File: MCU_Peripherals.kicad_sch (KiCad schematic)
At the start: 108 parts, among them J1 Conn_02x04_Odd_Even, J101 Conn_01x06_Male, J102 Conn_01x06_Male, J2 DS1023-2*8SF11, J20 DS1023-2*8SF11, J200 Conn_ARM_JTAG_SWD_10, J4 Conn_ARM_JTAG_SWD_10, J5 Conn_01x03_Female, J6 Conn_01x02, Q1 IRLR8726TRPBF, Q10 IRLR8726TRPBF, Q2 IRLR8726TRPBF, Q3 IRLR8726TRPBF, Q4 IRLR8726TRPBF, Q5 IRLR8726TRPBF, Q6 IRLR8726TRPBF, Q7 IRLR8726TRPBF, Q8 IRLR8726TRPBF, Q9 IRLR8726TRPBF, U1 STM32F103C8Tx, U10 AT24C16D-XHM-B, U101 TC4427, U102 TC4427, U103 TC4427, U104 TC4427, U105 TC4427, U2 STM32G030C6Tx, U3 MAX3485, Y1 16MHz, Y2 32.768KHz

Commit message: Cleaned up messy reference numbering Added labels to schematic
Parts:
- added R17: 10k, Resistor_SMD:R_0402_1005Metric, symbol Device:R_Small
- renumbered C200 to C10, C30 to C13, C31 to C14, C301 to C15, C9 to C16, C10 to C501, C300 to C9, D30 to D11, J102 to J10, J6 to J2, J1 to J3, J2 to J4, J20 to J5, J5 to J6, J4 to J7, J200 to J8, J101 to J9, R9 to R10, R10 to R11, R200 to R12, R201 to R13, R600 to R14, R601 to R15, R602 to R16, R35 to R8, R8 to R9, U10 to U3, U3 to U4
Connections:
- net GND: now also R17.2
- net LED1: now also U1.14 (PA4)
- net LED2: now also U1.15 (PA5)
- net LED3: now also U2.43 (PB4)
- net at U3.7 (WP): now also R17.1
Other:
- note added: "2.54mm, THT"
- note added: "Clock speed: 64MHz SPI Slave 16MHz crystal 8MHz clock output for MCU1"
- note added: "Clock speed: 72MHz SPI Master RTC crystal 8MHz clock from MCU2"
- note added: "Designed baud rate: 2M ESD protected"
- note added: "Failsafe RC element"
- note added: "Inter-board connectors"
- note added: "M2_USART2_RX"
- note added: "M2_USART2_TX"
- note added: "MCU 1"
- note added: "MCU 2"
- note added: "Output stages & Connectors"
- note added: "RS485 transciever"
- note added: "SWD/Debug connectors"
- moved on the sheet: C1, C13, C14, C15, C2, C3, C4, C5, C501, C6, C7, D20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

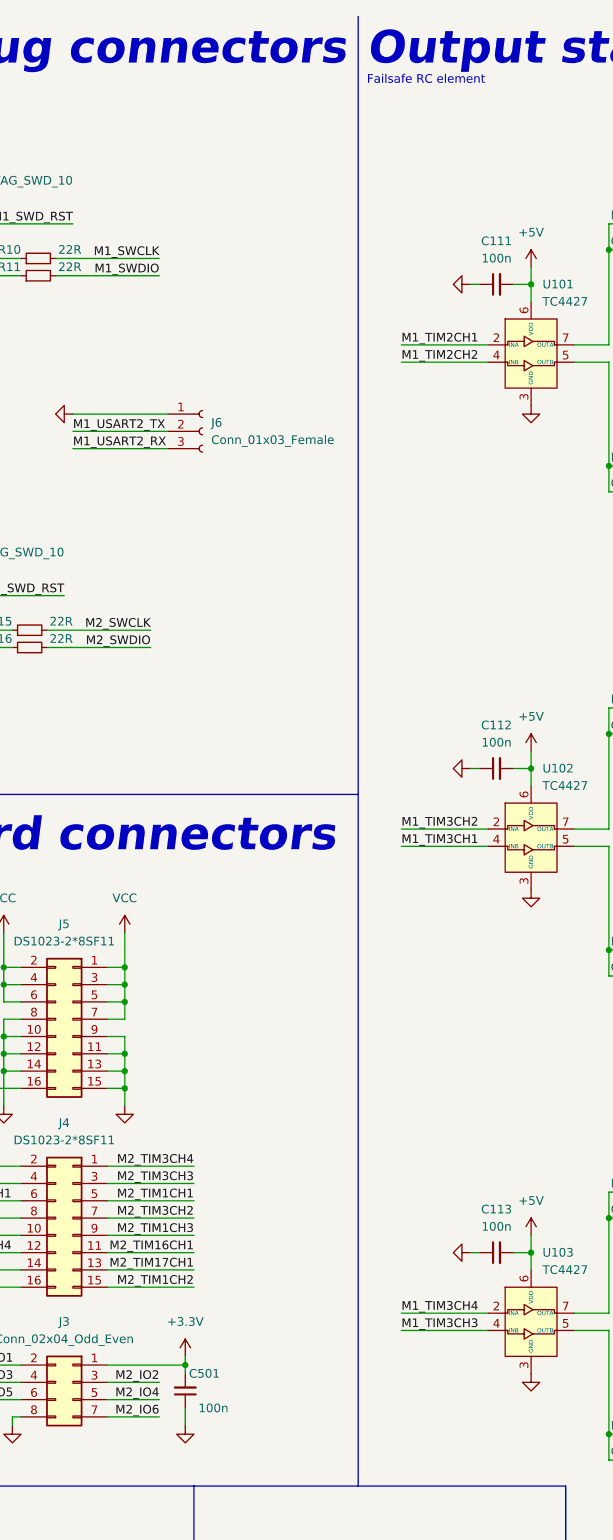
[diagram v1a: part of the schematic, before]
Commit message: Added FET driver cap
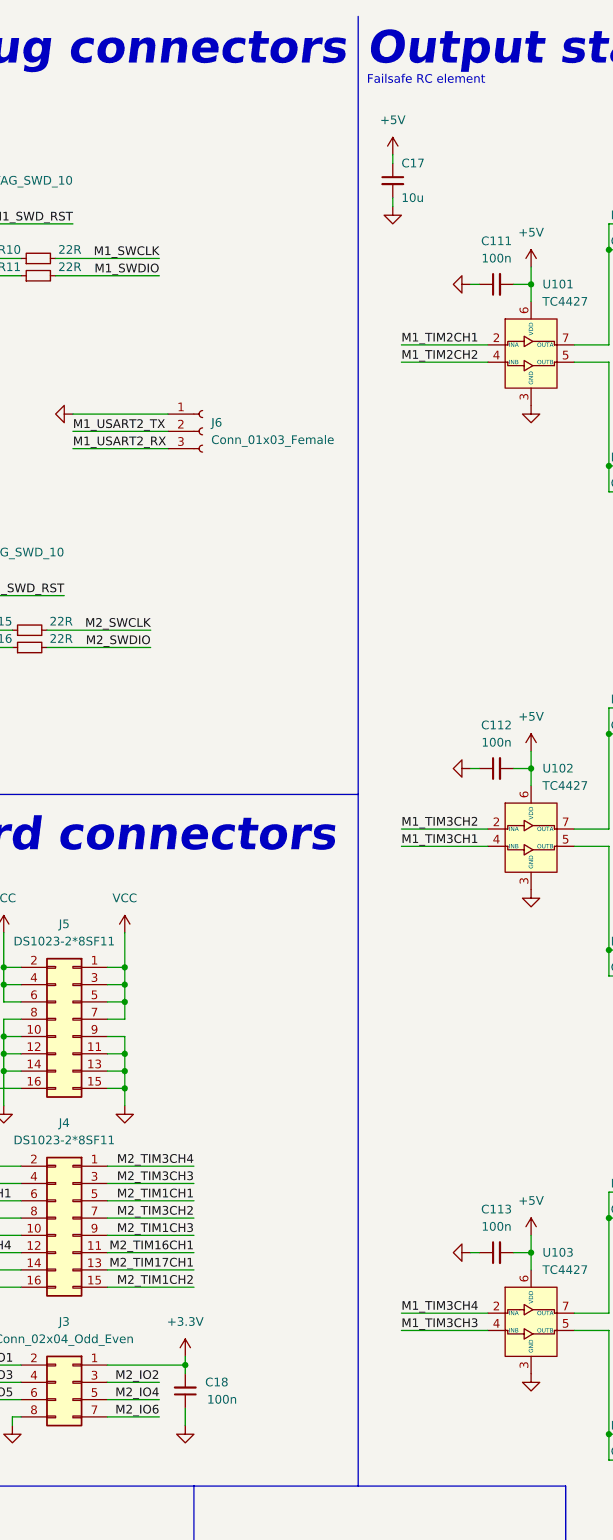
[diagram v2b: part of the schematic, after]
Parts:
- added C17: 10u, Resistor_SMD:R_1206_3216Metric, symbol Device:C_Small
- renumbered C501 to C18
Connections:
- net +5V: now also C17.1
- net GND: now also C17.2
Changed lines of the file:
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@@
     (stroke (width 0) (type default) (color 0 0 0 0))
   )
+  (wire (pts (xy 245.11 40.64) (xy 245.11 39.37))
+    (stroke (width 0) (type default) (color 0 0 0 0))
+  )
   (wire (pts (xy 80.01 105.41) (xy 95.25 105.41))
     (stroke (width 0) (type default) (color 0 0 0 0))
@@
     (stroke (width 0) (type default) (color 0 0 0 0))
   )
+  (wire (pts (xy 245.11 34.29) (xy 245.11 33.02))
+    (stroke (width 0) (type default) (color 0 0 0 0))
+  )
   (wire (pts (xy 229.87 270.51) (xy 229.87 273.05))
     (stroke (width 0) (type default) (color 0 0 0 0))
@@
     (pin "7")
   )
+  (symbol (lib_id "power:GND") (at 245.11 40.64 0) (unit 1)
+    (in_bom yes) (on_board yes) (fields_autoplaced)
+    (property "Reference" "#PWR0186" (id 0) (at 245.11 46.99 0)
+      (effects (font (size 1.27 1.27)) hide)
+    )
+    (property "Value" "GND" (id 1) (at 245.11 45.72 0)
+      (effects (font (size 1.27 1.27)) hide)
+    )
+    (property "Footprint" "" (id 2) (at 245.11 40.64 0)
+      (effects (font (size 1.27 1.27)) hide)
+    )
+    (property "Datasheet" "" (id 3) (at 245.11 40.64 0)
+      (effects (font (size 1.27 1.27)) hide)
+    )
+    (pin "1")
+  )
   (symbol (lib_id "Device:Q_NMOS_GDS") (at 378.46 153.67 0) (unit 1)
     (in_bom yes) (on_board yes) (fields_autoplaced)
@@
     (pin "3")
   )
+  (symbol (lib_id "Device:C_Small") (at 245.11 36.83 0) (unit 1)
+    (in_bom yes) (on_board yes)
+    (property "Reference" "C17" (id 0) (at 246.38 34.29 0)
+      (effects (font (size 1.27 1.27)) (justify left))
+    )
+    (property "Value" "10u" (id 1) (at 246.38 39.37 0)
+      (effects (font (size 1.27 1.27)) (justify left))
+    )
+    (property "Footprint" "Resistor_SMD:R_1206_3216Metric" (id 2) (at 245.11 36.83 0)
+      (effects (font (size 1.27 1.27)) hide)
+    )
+    (property "Datasheet" "~" (id 3) (at 245.11 36.83 0)
+      (effects (font (size 1.27 1.27)) hide)
+    )
+    (pin "1")
+    (pin "2")
+  )
   (symbol (lib_id "Device:Q_NMOS_GDS") (at 378.46 46.99 0) (unit 1)
     (in_bom yes) (on_board yes) (fields_autoplaced)
@@
   (symbol (lib_id "Device:C_Small") (at 214.63 214.63 180) (unit 1)
     (in_bom yes) (on_board yes)
-    (property "Reference" "C501" (id 0) (at 219.71 212.09 0)
+    (property "Reference" "C18" (id 0) (at 220.98 213.36 0)
       (effects (font (size 1.27 1.27)) (justify left))
     )
-    (property "Value" "100n" (id 1) (at 220.98 217.17 0)
+    (property "Value" "100n" (id 1) (at 222.25 215.9 0)
       (effects (font (size 1.27 1.27)) (justify left))
     )
@@
     (pin "2")
   )
+  (symbol (lib_id "power:+5V") (at 245.11 33.02 0) (unit 1)
+    (in_bom yes) (on_board yes) (fields_autoplaced)
+    (property "Reference" "#PWR0185" (id 0) (at 245.11 36.83 0)
+      (effects (font (size 1.27 1.27)) hide)
+    )
+    (property "Value" "+5V" (id 1) (at 245.11 27.94 0))
+    (property "Footprint" "" (id 2) (at 245.11 33.02 0)
+      (effects (font (size 1.27 1.27)) hide)
+    )
+    (property "Datasheet" "" (id 3) (at 245.11 33.02 0)
+      (effects (font (size 1.27 1.27)) hide)
+    )
+    (pin "1")
+  )
   (symbol (lib_id "Device:C_Small") (at 38.1 53.34 0) (unit 1)

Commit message: Ready for prod
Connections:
- no-connect marks 4 -> 20
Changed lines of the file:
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@@
   )
   (no_connect (at 184.15 107.95))
+  (no_connect (at 143.51 191.77))
+  (no_connect (at 95.25 82.55))
+  (no_connect (at 95.25 67.31))
+  (no_connect (at 95.25 62.23))
   (no_connect (at 185.42 53.34))
   (no_connect (at 185.42 55.88))
+  (no_connect (at 95.25 107.95))
+  (no_connect (at 95.25 110.49))
+  (no_connect (at 95.25 113.03))
+  (no_connect (at 95.25 115.57))
   (no_connect (at 184.15 110.49))
+  (no_connect (at 95.25 217.17))
+  (no_connect (at 128.27 189.23))
+  (no_connect (at 128.27 176.53))
+  (no_connect (at 128.27 173.99))
+  (no_connect (at 128.27 201.93))
+  (no_connect (at 128.27 204.47))
+  (no_connect (at 128.27 207.01))
+  (no_connect (at 128.27 227.33))
   (wire (pts (xy 345.44 123.19) (xy 345.44 125.73))
     (stroke (width 0) (type default) (color 0 0 0 0))
